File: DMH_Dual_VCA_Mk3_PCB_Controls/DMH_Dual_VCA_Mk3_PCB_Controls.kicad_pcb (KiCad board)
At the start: 2 copper layers, 49 x 121 mm, 38 parts, among them J14 Conn_01x06, J15 Conn_01x08, J16 Conn_01x06, J24 Conn_01x08, SW1 SW_DPDT_3way, SW2 SW_DPDT_OnOffOn_x2, U9 TL074

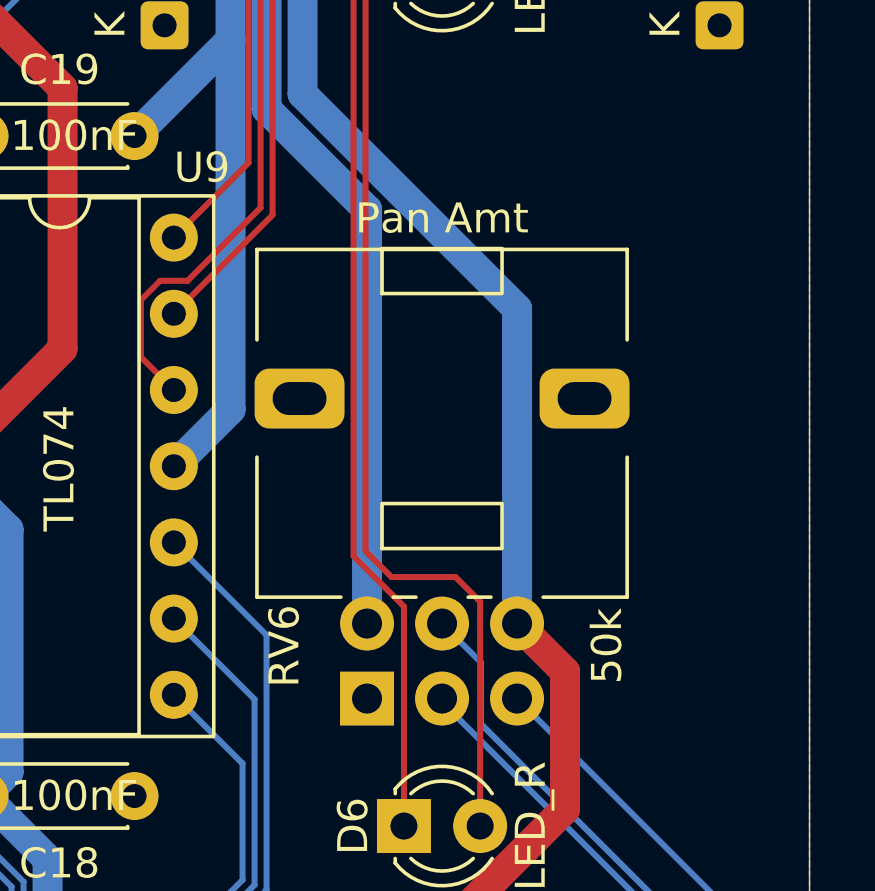
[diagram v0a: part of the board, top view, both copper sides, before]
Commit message: Fixed Alps RK09L pot 3D model
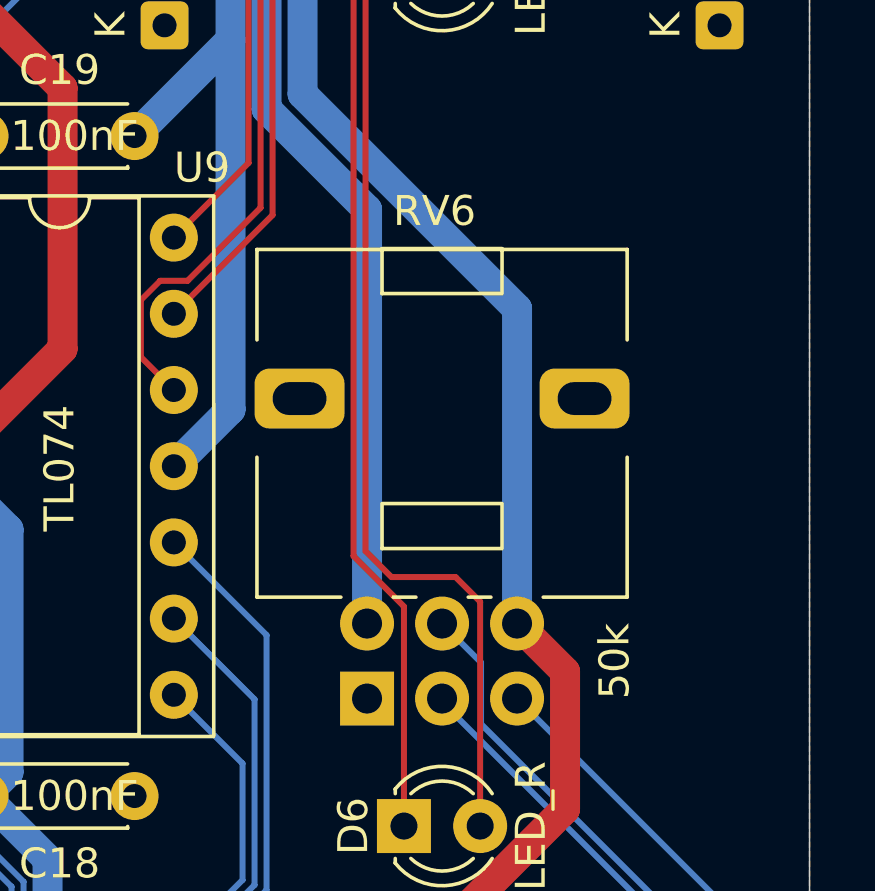
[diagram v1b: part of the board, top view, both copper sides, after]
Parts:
- RV6: footprint Potentiometer_THT:Potentiometer_Alps_RK09L_Double_Vertical -> SynthStuff:Potentiometer_Alps_RK09L_Double_Vertical
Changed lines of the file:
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@@
 		)
 	)
-	(footprint "Potentiometer_THT:Potentiometer_Alps_RK09L_Double_Vertical"
+	(footprint "SynthStuff:Potentiometer_Alps_RK09L_Double_Vertical"
 		(locked yes)
 		(layer "F.Cu")
@@
 		(tags "Potentiometer vertical Alps RK09L Double")
 		(property "Reference" "RV6"
-			(at 1.75 -2.75 90)
+			(at 16.25 2.25 180)
 			(layer "F.SilkS")
 			(effects
@@
 		)
 		(property "Value" "50k"
-			(at 1.75 8 90)
+			(at 1.25 8.25 90)
 			(layer "F.SilkS")
 			(effects
@@
 		)
 		(property "Function" "Pan Amt"
-			(at 16 2.5 0)
-			(unlocked yes)
-			(layer "F.SilkS")
+			(at 0 0 90)
+			(unlocked yes)
+			(layer "F.Fab")
+			(hide yes)
 			(effects
 				(font
@@
 		)
 		(fp_text user "${REFERENCE}"
-			(at 4.5 2.5 0)
+			(at 4.5 2.5 180)
 			(layer "F.Fab")
 			(effects
@@
 		(embedded_fonts no)
 		(model "${KICAD10_3DMODEL_DIR}/Potentiometer_THT.3dshapes/Potentiometer_Alps_RK09L_Double_Vertical.step"
+			(hide yes)
 			(offset
 				(xyz 0 0 0)
@@
 			)
 		)
+		(model "${KIPRJMOD}/../Libraries/SynthStuff/3D_models/RK09L12-F15V.STEP"
+			(offset
+				(xyz 10 -2.5 7.5)
+			)
+			(scale
+				(xyz 1 1 1)
+			)
+			(rotate
+				(xyz -0 -0 90)
+			)
+		)
